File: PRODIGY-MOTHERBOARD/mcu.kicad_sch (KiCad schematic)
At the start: 9 parts, among them J11 Bus_M.2_Socket_A

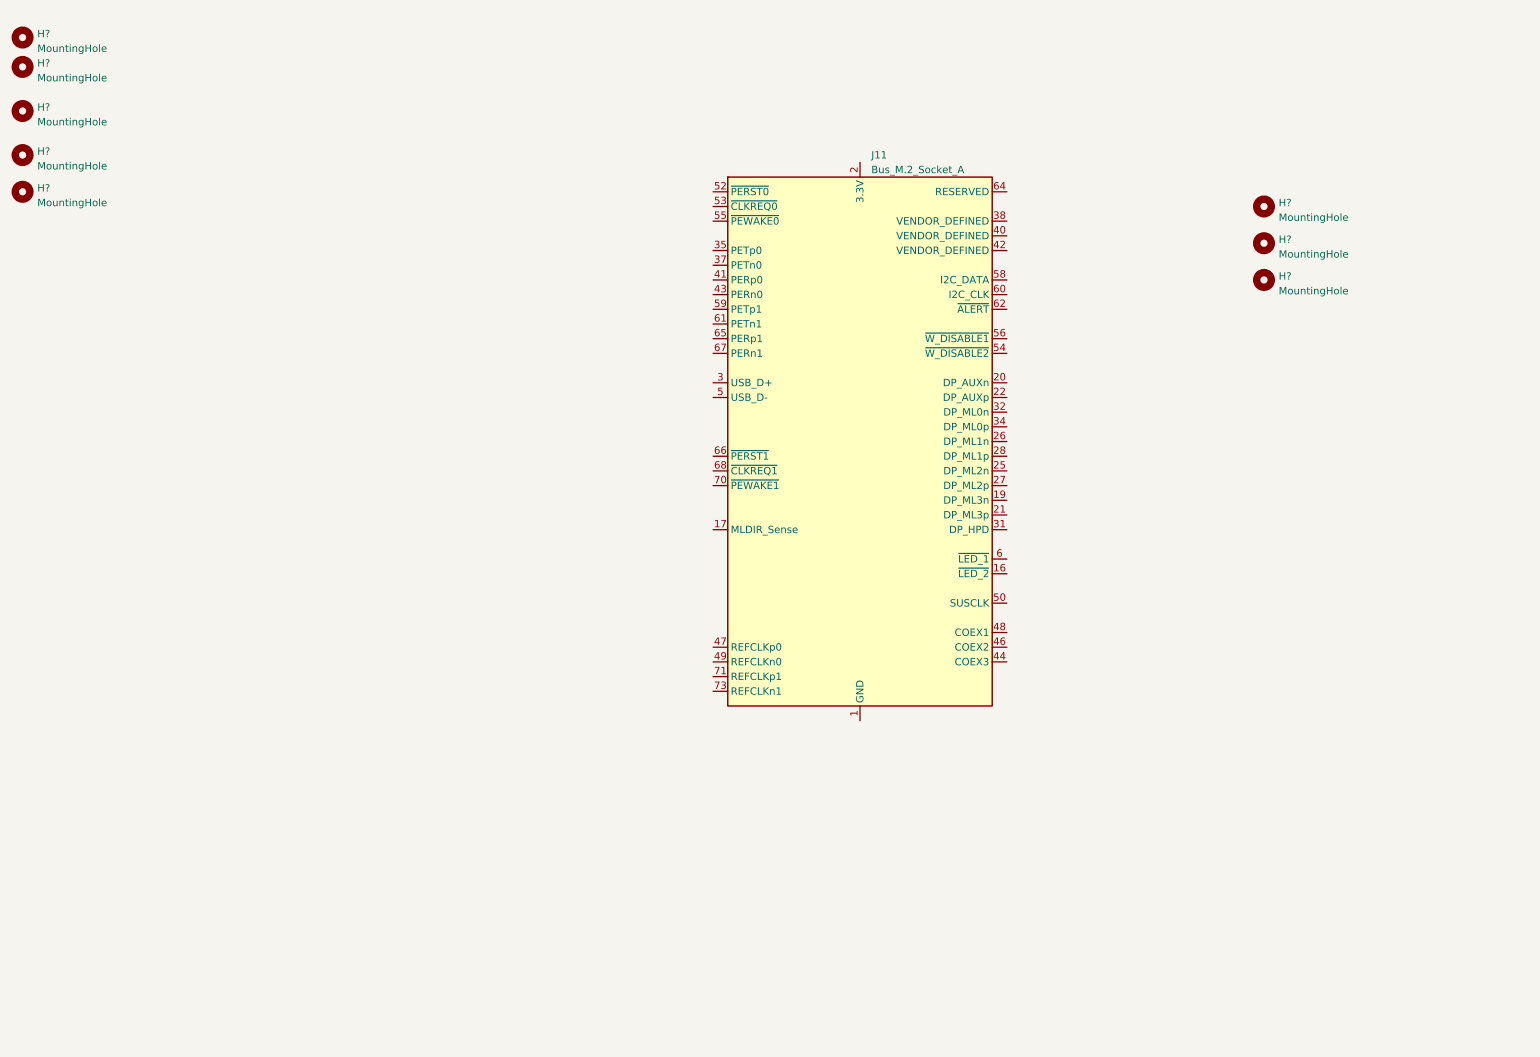
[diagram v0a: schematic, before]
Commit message: project restructure done. Hierarchical sheet done. Outputs/breakouts sheet done
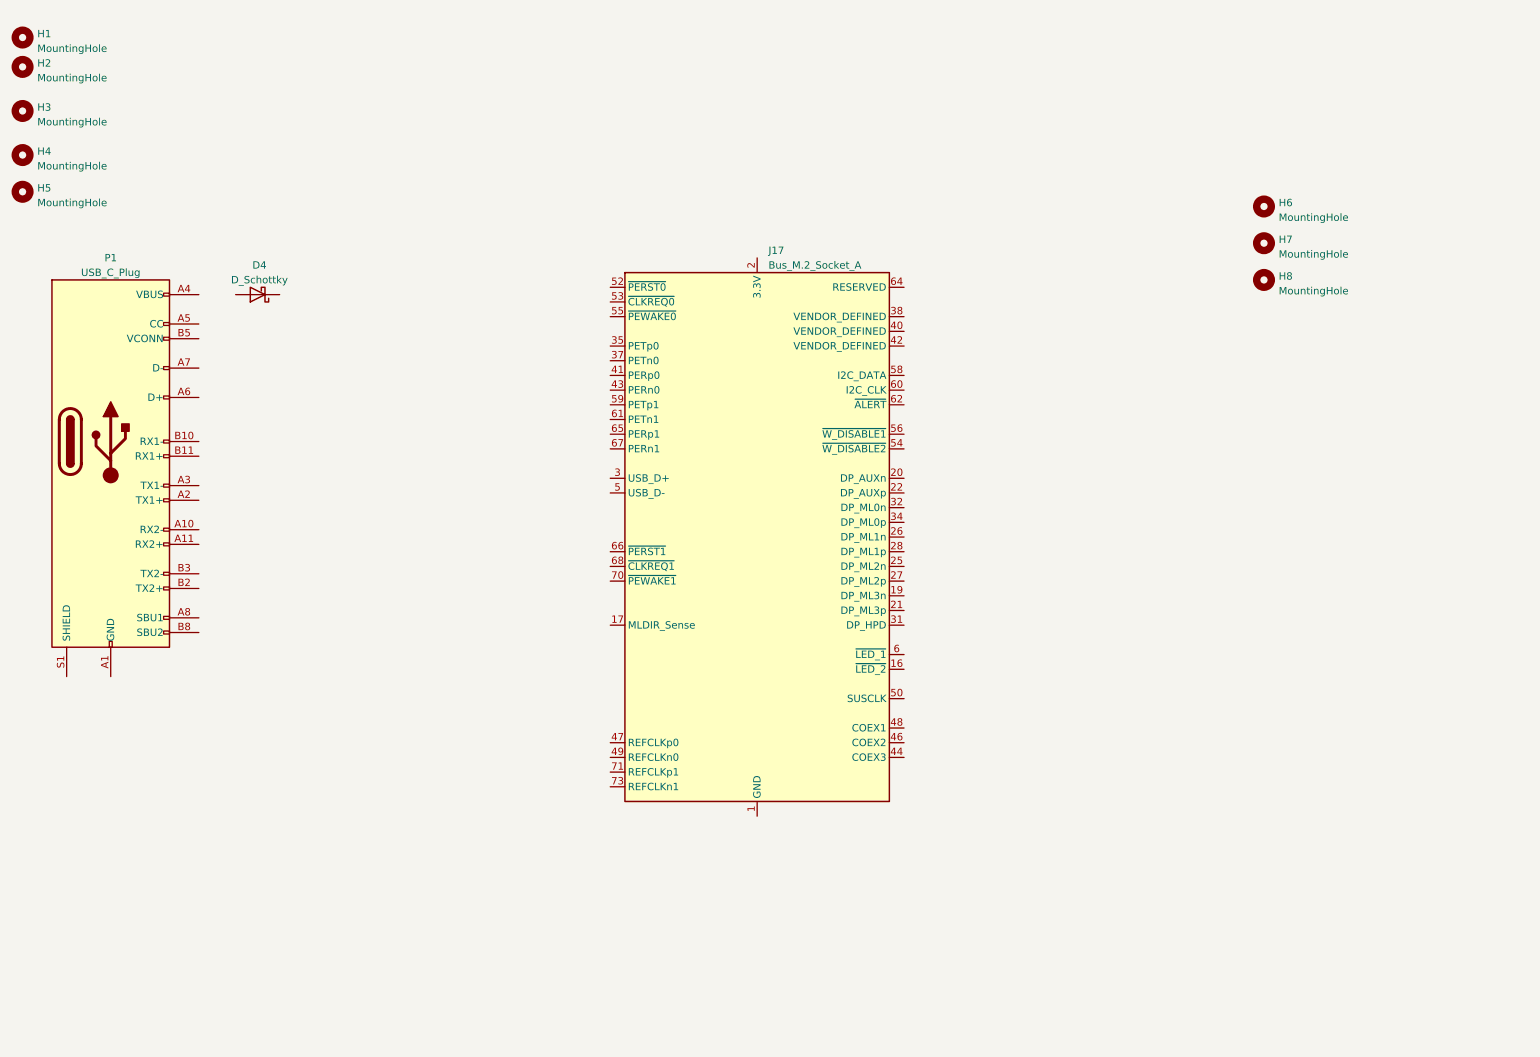
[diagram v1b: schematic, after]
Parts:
- added D4: D_Schottky, Diode_SMD:D_SMB, symbol Device:D_Schottky
- added P1: USB_C_Plug, Connector_USB:USB_C_Receptacle_GCT_USB4105-xx-A_16P_TopMnt_Horizontal, symbol Connector:USB_C_Plug
- gave numbers to parts that had none: 8
- renumbered J11 to J17
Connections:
- new net: P1.A1 (GND), P1.A12 (GND), P1.B1 (GND), P1.B12 (GND)
- new net: P1.A4 (VBUS), P1.A9 (VBUS), P1.B4 (VBUS), P1.B9 (VBUS)
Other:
- moved on the sheet: J17

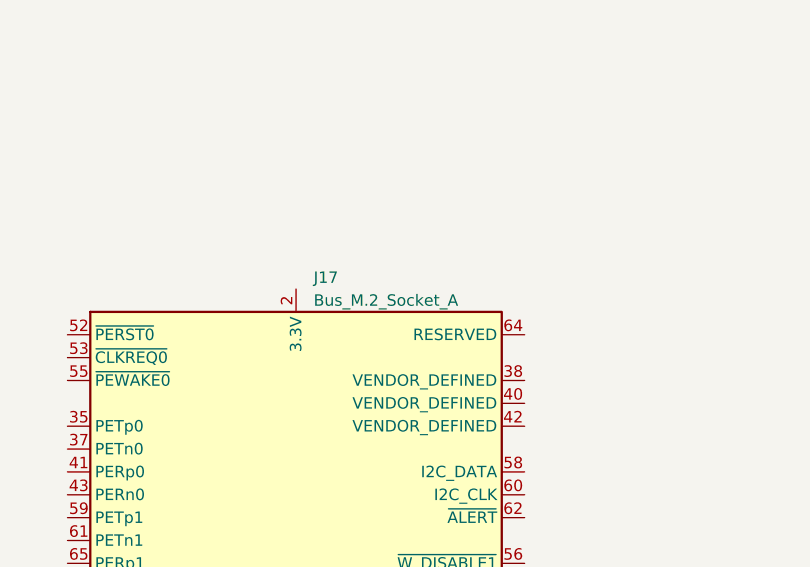
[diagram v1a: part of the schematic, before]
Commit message: SPI SD CARD circuit added.
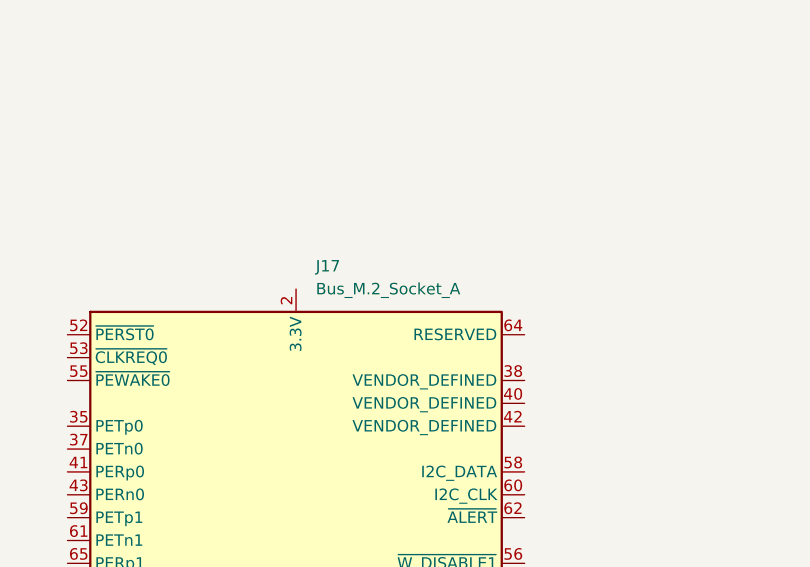
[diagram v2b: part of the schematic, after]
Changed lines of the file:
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@@
 		(fields_autoplaced yes)
 		(property "Reference" "J17"
-			(at 153.0859 59.69 0)
+			(at 153.3241 58.42 0)
 			(effects
 				(font
@@
 		)
 		(property "Value" "Bus_M.2_Socket_A"
-			(at 153.0859 62.23 0)
+			(at 153.3241 60.96 0)
 			(effects
 				(font

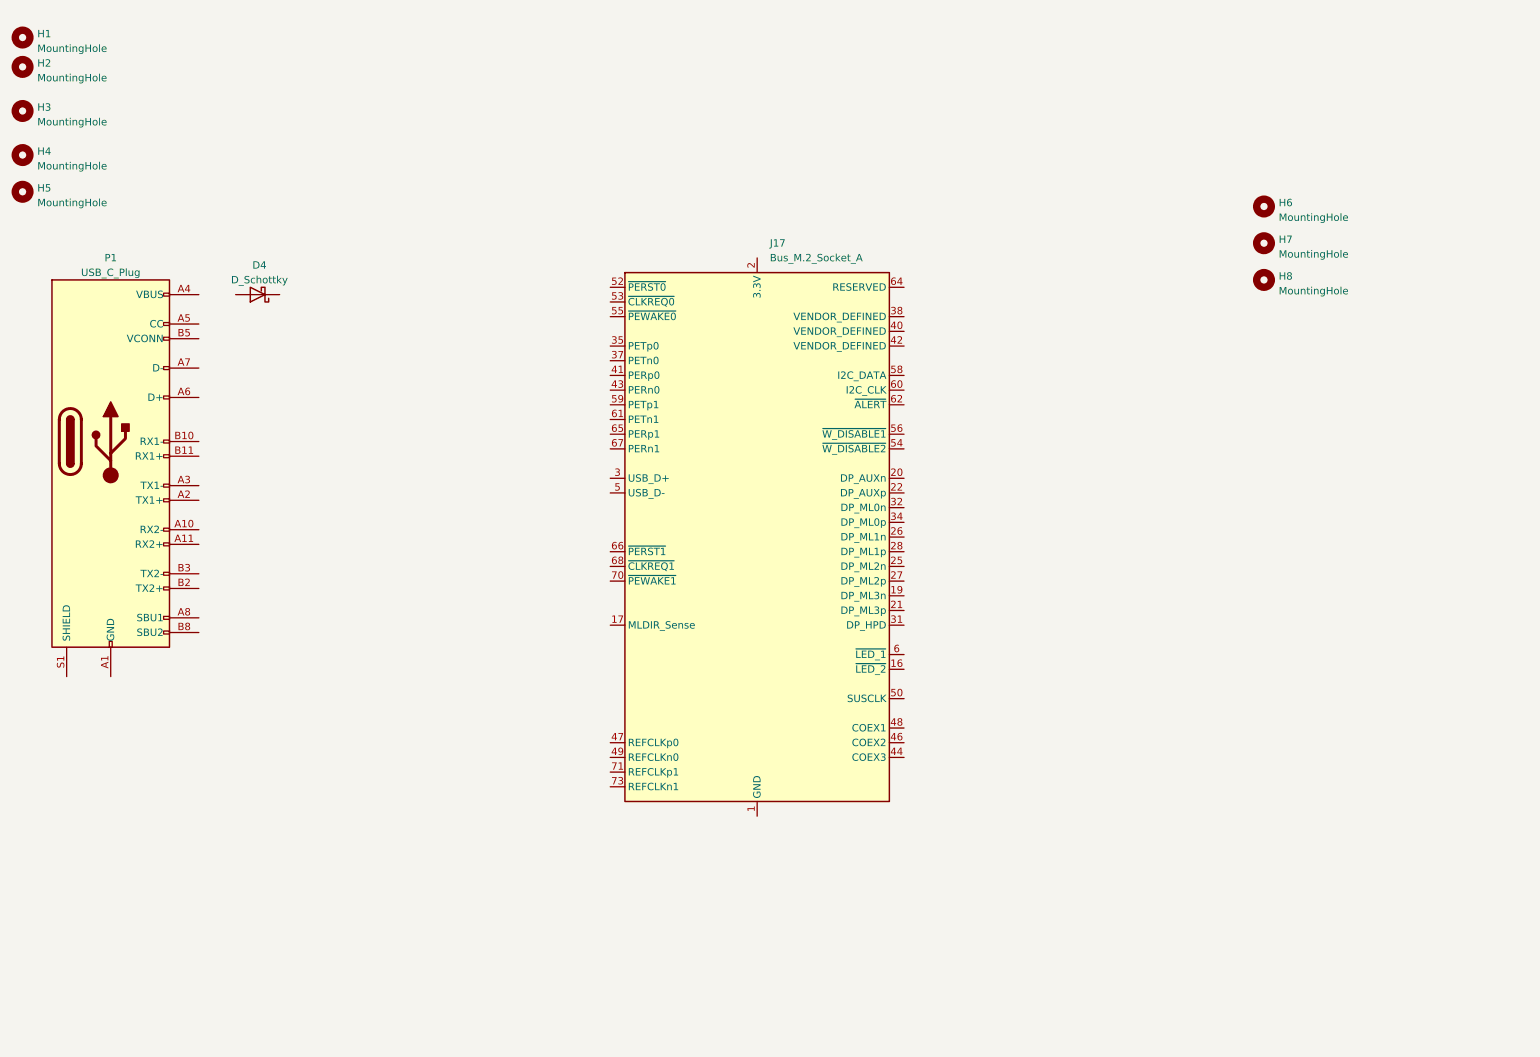
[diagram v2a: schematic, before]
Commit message: Finished neopixel and button's schematic.
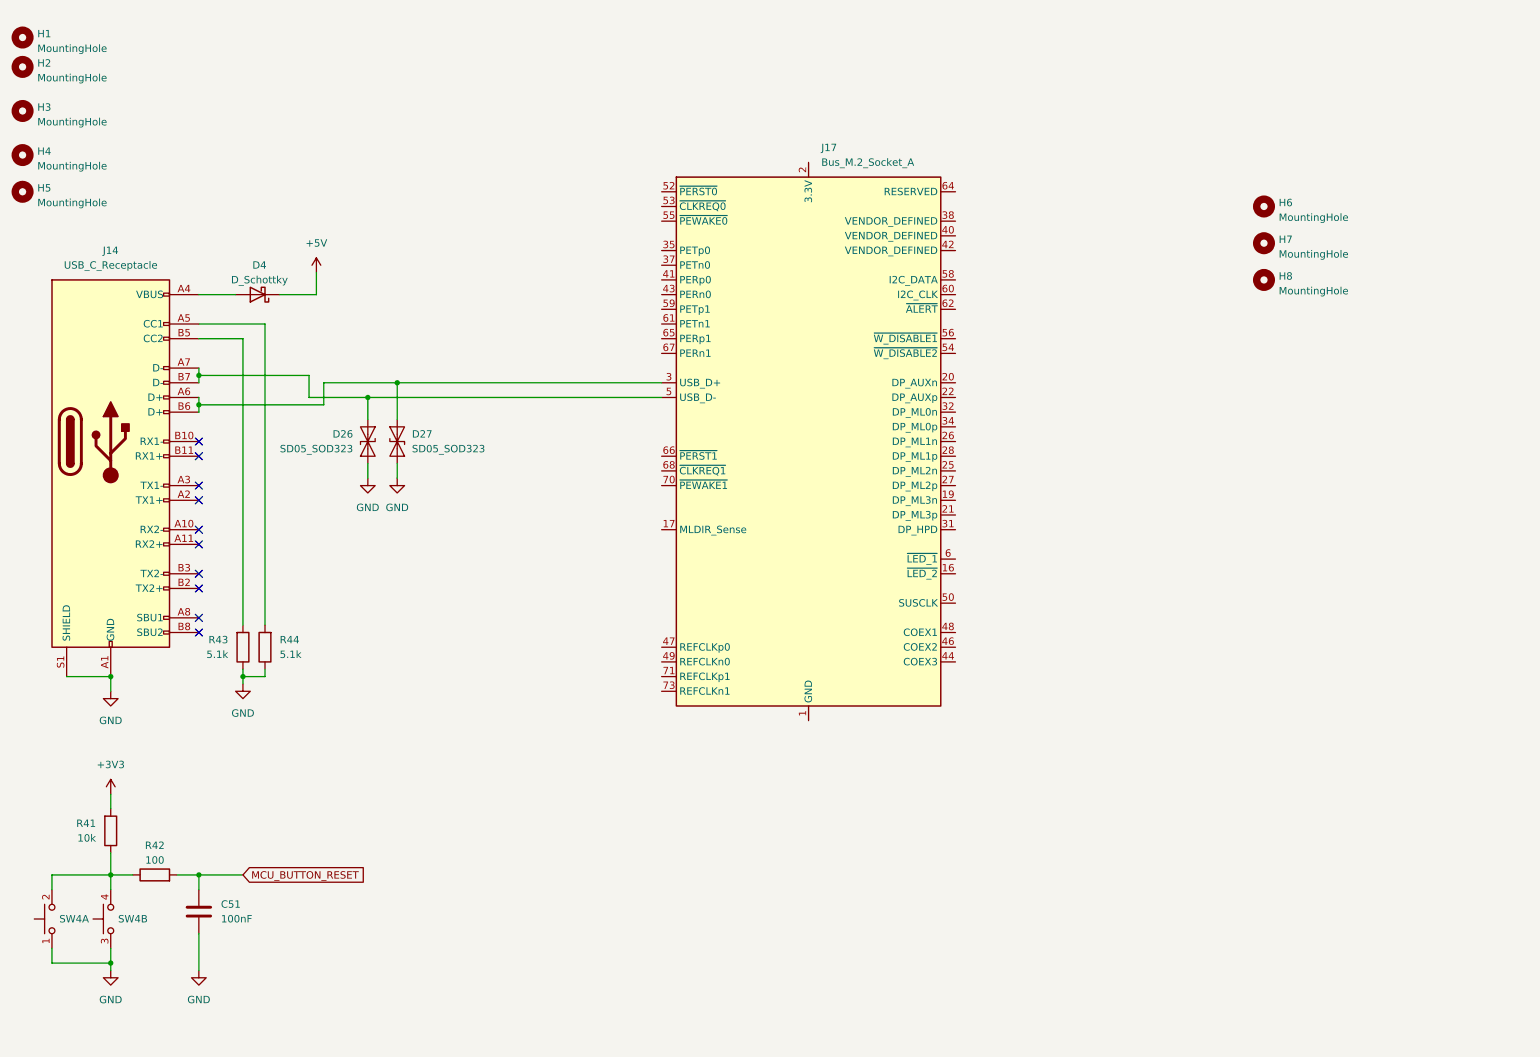
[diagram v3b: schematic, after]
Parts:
- removed P1: USB_C_Plug, Connector_USB:USB_C_Receptacle_GCT_USB4105-xx-A_16P_TopMnt_Horizontal, symbol Connector:USB_C_Plug
- added C51: 100nF, symbol Device:C
- added D26, D27: SD05_SOD323, Diode_SMD:D_SOD-323, symbol Diode:SD05_SOD323
- added J14: USB_C_Receptacle, symbol Connector:USB_C_Receptacle
- added R41: 10k, Resistor_SMD:R_0603_1608Metric, symbol Device:R
- added R42: 100, Resistor_SMD:R_0603_1608Metric, symbol Device:R
- added R43, R44: 5.1k, Resistor_SMD:R_0603_1608Metric, symbol Device:R
- added SW4: SW_Push_Dual_x2, symbol Switch:SW_Push_Dual_x2
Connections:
- net at J17.3 (USB_D+): now also D27.2 (A2), J14.A6 (D+), J14.B6 (D+)
- net at J17.5 (USB_D-): now also D26.2 (A2), J14.A7 (D-), J14.B7 (D-)
- net +5V: now reaches D4.1 (K)
- net at D4.2 (A): now also J14.A4 (VBUS), J14.A9 (VBUS), J14.B4 (VBUS), J14.B9 (VBUS)
- new net: R41.1, R42.1, SW4.2 (D), SW4.4 (D)
- new net: J14.A5 (CC1), R44.2
- new net: J14.B5 (CC2), R43.2
- new net +3V3: R41.2
- new net GND: C51.2, D26.1 (A1), D27.1 (A1), J14.A1 (GND), J14.A12 (GND), J14.B1 (GND), J14.B12 (GND), J14.S1 (SHIELD), R43.1, R44.1, SW4.1 (C), SW4.3 (C)
- new net MCU_BUTTON_RESET: C51.1, R42.2
- no-connect marks 0 -> 10
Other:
- moved on the sheet: J17

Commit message: CAN schematic done
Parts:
- removed J17: Bus_M.2_Socket_A, m.2_edge_connector_key_a:121992304, symbol Connector:Bus_M.2_Socket_A
- added J28: Bus_M.2_Socket_B, symbol Connector:Bus_M.2_Socket_B
- renumbered C51 to C1, D4 to D1, D26 to D2, D27 to D3, J14 to J1, R41 to R1, R42 to R2, R43 to R3, R44 to R4, SW4 to SW1
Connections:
- net MCU_BUTTON_RESET: now also J28.67 (~{RESET})
- net at D2.2 (A2), J1.A7 (D-), J1.B7 (D-): now also J28.9 (USB_D-)
- net at D3.2 (A2), J1.A6 (D+), J1.B6 (D+): now also J28.7 (USB_D+)
- new net: J28.11 (GND), J28.27 (GND), J28.3 (GND), J28.33 (GND), J28.39 (GND), J28.45 (GND), J28.5 (GND), J28.51 (GND), J28.57 (GND), J28.71 (GND), J28.73 (GND)
- new net: J28.2 (3.3V), J28.4 (3.3V), J28.70 (3.3V), J28.72 (3.3V), J28.74 (3.3V)
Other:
- moved on the sheet: C1, R1, R2, SW1A, SW1B

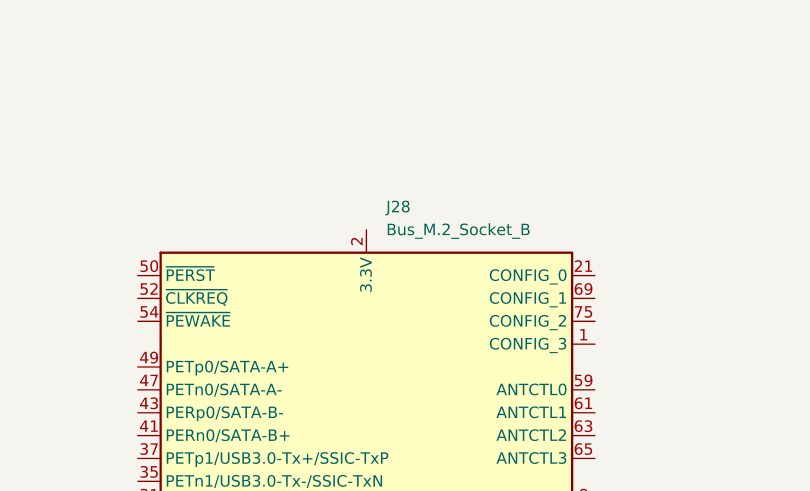
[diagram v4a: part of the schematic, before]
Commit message: SPI NFC schematic done.
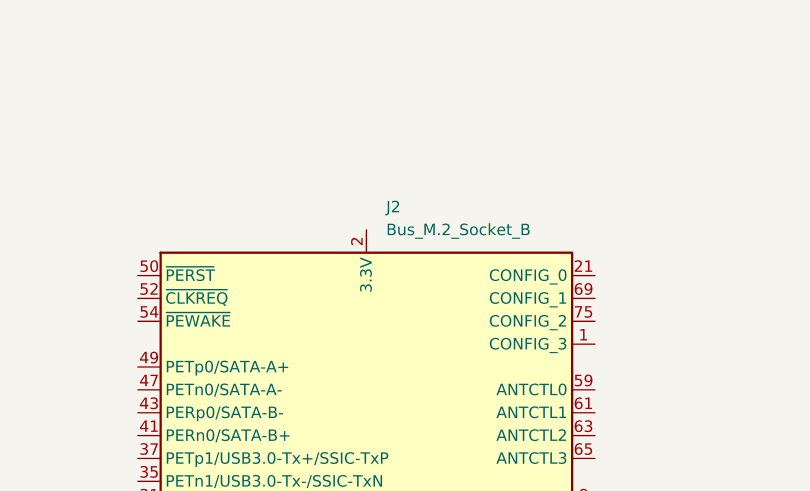
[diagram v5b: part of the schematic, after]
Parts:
- renumbered J28 to J2
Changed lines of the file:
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@@
 		(dnp no)
 		(fields_autoplaced yes)
-		(property "Reference" "J28"
+		(property "Reference" "J2"
 			(at 168.5641 41.91 0)
 			(effects
@@
 			(project "PRODIGY-MOTHERBOARD"
 				(path "/f1c25860-8989-4190-bd24-2491d23ca7d9/27fc7bb4-2bbd-477b-b6e3-e07582947566"
-					(reference "J28")
+					(reference "J2")
 					(unit 1)
 				)
